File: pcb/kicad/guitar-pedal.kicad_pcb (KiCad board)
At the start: 2 copper layers, 100 parts, among them J301 TagConnect_TC2030, U201 HT7533-1, U202 TLV62569DBV, U203 MCP6001-OT, U301 STM32F401RBTx, U501 USBLC6-2SC6, U601 REF3033, U603 MCP6001-OT, U605 MCP6001-OT, U606 MCP6001-OT

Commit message: Added PCB layout and fabrication output.
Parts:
- added D301: ~, pedal-components:PESD3V3L1BA, F.Cu at (182.6, 57.7)
- added D302: ~, pedal-components:PESD3V3L1BA, F.Cu at (182.6, 54.6)
- added D303: ~, pedal-components:PESD3V3L1BA, F.Cu at (177.7, 64.6)
- added D304: ~, pedal-components:PESD3V3L1BA, F.Cu at (182.6, 59.4)
- added D305: ~, pedal-components:PESD3V3L1BA, F.Cu at (173.7, 64.5)
- added D401: ~, pedal-components:PESD3V3L1BA, F.Cu at (114.6, 107.4)
- added D402: ~, pedal-components:PESD3V3L1BA, F.Cu at (114.1, 129.3)
- added D403: ~, pedal-components:PESD3V3L1BA, F.Cu at (184.4, 123.7)
- added D404: ~, pedal-components:PESD3V3L1BA, F.Cu at (113.4, 121.2)
- added D405: ~, pedal-components:PESD3V3L1BA, F.Cu at (113.3, 141.0)
- added D601: ~, pedal-components:PESD3V3L1BA, F.Cu at (128.3, 64.3)
- added D602: ~, pedal-components:PESD3V3L1BA, F.Cu at (102.6, 64.3)
- added H101: MountingHole, MountingHole:MountingHole_3.2mm_M3_DIN965_Pad, F.Cu at (103.0, 102.0)
- added H102: MountingHole, MountingHole:MountingHole_3.2mm_M3_DIN965_Pad, F.Cu at (199.0, 86.0)
- added H103: MountingHole, MountingHole:MountingHole_3.2mm_M3_DIN965_Pad, F.Cu at (198.0, 135.0)
- added H104: MountingHole, MountingHole:MountingHole_3.2mm_M3_DIN965_Pad, F.Cu at (158.0, 54.0)
- added H105: MountingHole, MountingHole:MountingHole_3.2mm_M3_DIN965_Pad, F.Cu at (199.0, 54.0)
- added J501: USB4105-GF-A, Connector_USB:USB_C_Receptacle_GCT_USB4105-xx-A_16P_TopMnt_Horizontal, F.Cu at (202.5, 67.4)
- added J601: NMJ4HCD2, pedal-components:NMJ4HCD2, F.Cu at (140.0, 47.6)
- added J602: NMJ4HCD2, pedal-components:NMJ4HCD2, F.Cu at (114.0, 47.6)
- added L202: 68u, pedal-components:ASPI-4030S-680M-T, F.Cu at (195.4, 98.6)
- added RV401: 50K Linear, pedal-components:PTV09A-4030S-A503, F.Cu at (131.1, 115.9)
- added RV402: 50K Linear, pedal-components:PTV09A-4030S-A503, F.Cu at (149.7, 115.9)
- added RV403: 50K Linear, pedal-components:PTV09A-4030S-A503, F.Cu at (168.5, 115.9)
- added RV404: 50K Linear, pedal-components:PTV09A-4030S-A503, F.Cu at (131.1, 136.0)
- added RV405: 50K Linear, pedal-components:PTV09A-4030S-A503, F.Cu at (149.7, 136.0)
- added RV406: 50K Linear, pedal-components:PTV09A-4030S-A503, F.Cu at (168.5, 136.0)
- added SW401: PBS-24-202P, pedal-components:FSW-DPDT-020, F.Cu at (195.6, 121.2)
- added SW402: LP4EE1PBCTR, pedal-components:LP4EE1PBCTR, F.Cu at (114.6, 115.9)
- added SW403: LP4EE1PBCTR, pedal-components:LP4EE1PBCTR, F.Cu at (114.6, 135.7)
- added U602: DAC7563SDGSR, pedal-components:10-VSSOP-TI, F.Cu at (109.6, 93.4)
- added U604: ADC141S626, pedal-components:10-VSSOP-TI, F.Cu at (141.3, 94.1)
- added Y301: 16MHz, pedal-components:RH100-16.000-8-2020-TR, F.Cu at (164.8, 85.6)
- moved R304 150.4 mm to (183.4, 70.4), turned to -90 degrees
- moved R203 148.7 mm to (200.2, 104.7), turned to -90 degrees
- moved R202 147.9 mm to (197.9, 104.7), turned to 90 degrees
- moved R303 146.6 mm to (179.7, 70.4), turned to -90 degrees
- moved C302 143.9 mm to (180.9, 97.5), turned to 180 degrees
- moved R306 143.4 mm to (176.5, 80.1), turned to -90 degrees
- moved R305 143.1 mm to (175.9, 70.4), turned to -90 degrees
- moved C301 142.5 mm to (179.0, 99.6)
- moved U202 140.3 mm to (199.6, 100.2), turned to -90 degrees
- moved C204 139.2 mm to (199.7, 96.6), turned to 180 degrees
- moved C309 139.2 mm to (185.6, 84.7), turned to -90 degrees
- moved R302 139.1 mm to (172.2, 70.5), turned to -90 degrees
- moved R301 136.3 mm to (167.9, 87.9)
- moved U301 135.8 mm to (177.4, 89.2)
- moved C207 135.7 mm to (195.6, 104.7), turned to -90 degrees
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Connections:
- net Net-(C308-Pad1) renamed /Processor/HSE_PRE_OUT
- net Net-(D302-A2) renamed /Processor/TAG_nRST
- net Net-(D303-A2) renamed /Processor/TAG_SWCLK
- net Net-(D304-A2) renamed /Processor/TAG_SWDIO
- net Net-(D305-A2) renamed /Processor/TAG_SWO
- net Net-(U203-+) renamed /PowerSupply/VCOM_INPUT
- net Net-(U301-BOOT0) renamed /Processor/BOOT0
- U301 pad 44: /USB/D- -> /Processor/D-
- U301 pad 45: /USB/D+ -> /Processor/D+
- U501 pad 1: /USB/D+ -> /Processor/D+
- U501 pad 3: /USB/D- -> /Processor/D-
- U501 pad 4: /USB/D- -> /USB/CONN_D-
- U501 pad 6: /USB/D+ -> /USB/CONN_D+
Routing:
- net +3V3: track 0.00 -> 445.1 mm, vias 0 -> 16
- net GND: track 0.00 -> 159.8 mm, vias 0 -> 204
- net +3.3VA: track 0.00 -> 136.7 mm, vias 0 -> 13
- net /Effect Controls/EFFECT2_EN: track 0.00 -> 115.0 mm
- net +5V: track 0.00 -> 109.6 mm, vias 0 -> 6
- net /Data Converters/DAC_NCLR: track 0.00 -> 102.9 mm, vias 0 -> 2
- net /Data Converters/DAC_NLDAC: track 0.00 -> 98.6 mm, vias 0 -> 2
- net /Effect Controls/EFFECT1_EN: track 0.00 -> 82.6 mm, vias 0 -> 2
- net /Data Converters/DAC_CS: track 0.00 -> 81.6 mm, vias 0 -> 2
- net /Data Converters/DAC_SCLK: track 0.00 -> 80.1 mm, vias 0 -> 2
- net /Data Converters/DAC_MOSI: track 0.00 -> 78.8 mm, vias 0 -> 2
- net /Effect Controls/EFFECT2_KNOB0: track 0.00 -> 66.1 mm
- net /Data Converters/ADC_NCS: track 0.00 -> 62.5 mm, vias 0 -> 2
- net /Data Converters/ADC_MISO: track 0.00 -> 61.0 mm, vias 0 -> 2
- net /Effect Controls/EFFECT1_KNOB0: track 0.00 -> 59.0 mm, vias 0 -> 2
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- added copper zone on B.Cu, net +3.3VA
- added copper zone on F.Cu, net +3.3VA
- added copper zone on B.Cu, net +3V3
- added copper zone on F.Cu, net +3V3
- added copper zone on B.Cu, net +5V
- added copper zone on F.Cu, net +5V
- added copper zone on F.Cu, net /PowerSupply/5V_FILT
- added copper zone on B.Cu, net GND
- added copper zone on F.Cu, net GND
- added copper zone on In1.Cu, net GND
- added copper zone on In2.Cu, net GND
- added copper zone on B.Cu, net VBUS
- added copper zone on F.Cu, net VBUS
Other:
- board outline added: 110 x 96 mm
- copper layers 2 -> 4
- board text added: "Effect 1 Enable"
- board text added: "Effect 1 Param 0"
- board text added: "Effect 1 Param 1"
- board text added: "Effect 1 Param 2"
- board text added: "Effect 2 Enable"
- board text added: "Effect 2 Param 0"
- board text added: "Effect 2 Param 1"
- board text added: "Effect 2 Param 2"
- board text added: "Input"
- board text added: "Output"

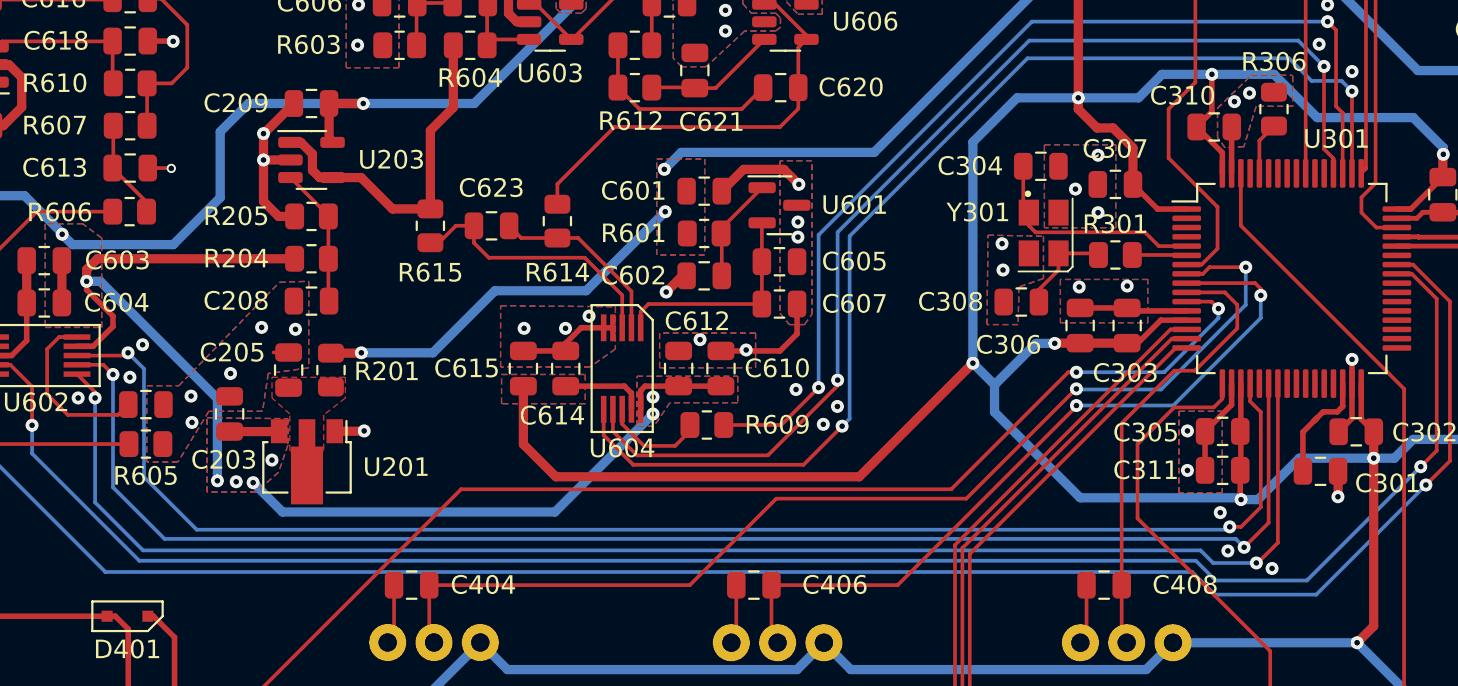
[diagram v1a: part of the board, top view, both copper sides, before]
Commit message: Update .ioc file and fix DAC pinout.
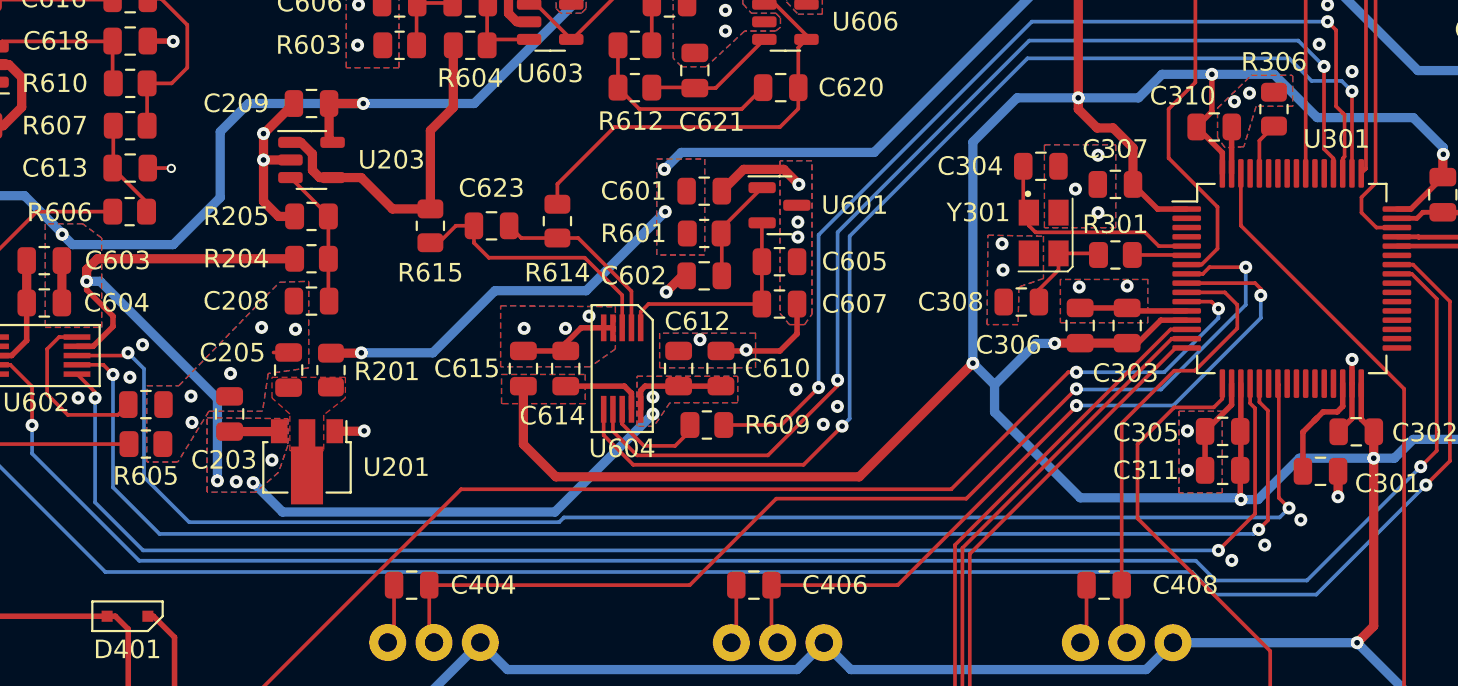
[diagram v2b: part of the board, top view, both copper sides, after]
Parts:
- C608: value 150p -> 100n
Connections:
- U301 pad 20: /Data Converters/DAC_MOSI -> /Data Converters/DAC_CS
- U301 pad 21: unconnected-(U301-PA5-Pad21) -> /Data Converters/DAC_SCLK
- U301 pad 22: /Data Converters/DAC_SCLK -> unconnected-(U301-PA6-Pad22)
- U301 pad 23: /Data Converters/DAC_CS -> /Data Converters/DAC_MOSI
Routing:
- net /Data Converters/DAC_CS: track 81.6 -> 79.0 mm
- net /Data Converters/DAC_MOSI: track 78.8 -> 80.0 mm
- net /Data Converters/DAC_SCLK: track 80.1 -> 79.5 mm
